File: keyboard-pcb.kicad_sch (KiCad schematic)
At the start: 3 parts, among them P1 USB_C_Plug_USB2.0, U1 RP2040, U2 XC6206PxxxMR

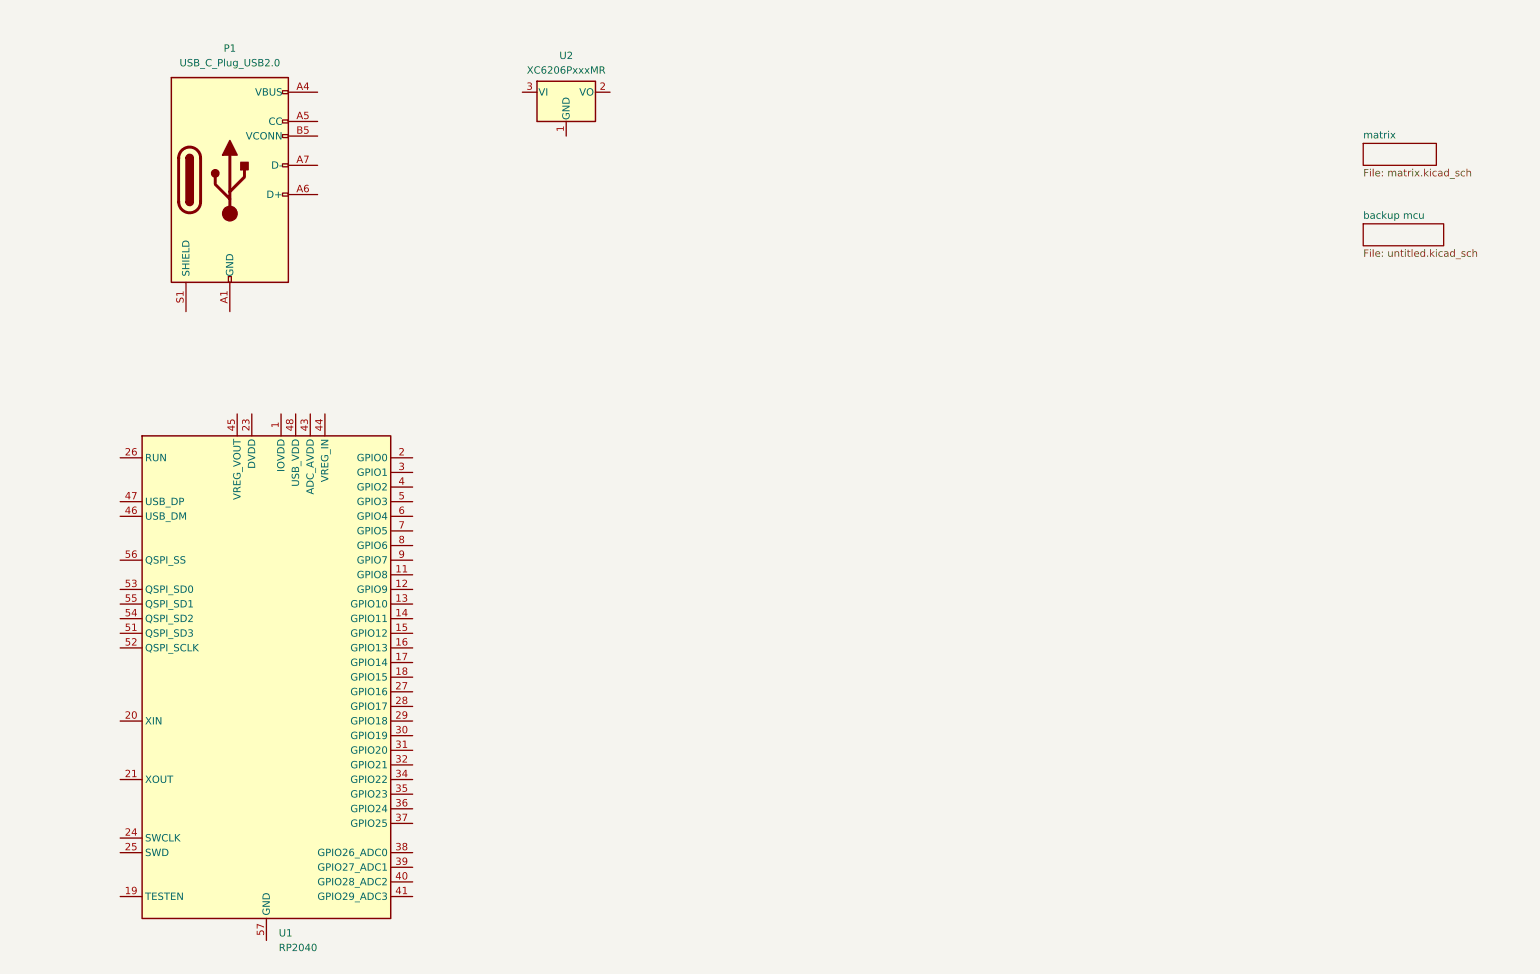
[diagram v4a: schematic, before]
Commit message: Assigned footprints to components
Also edited layout slightly (7u spacebar and removal of PrtSc, ScLk, Pause)
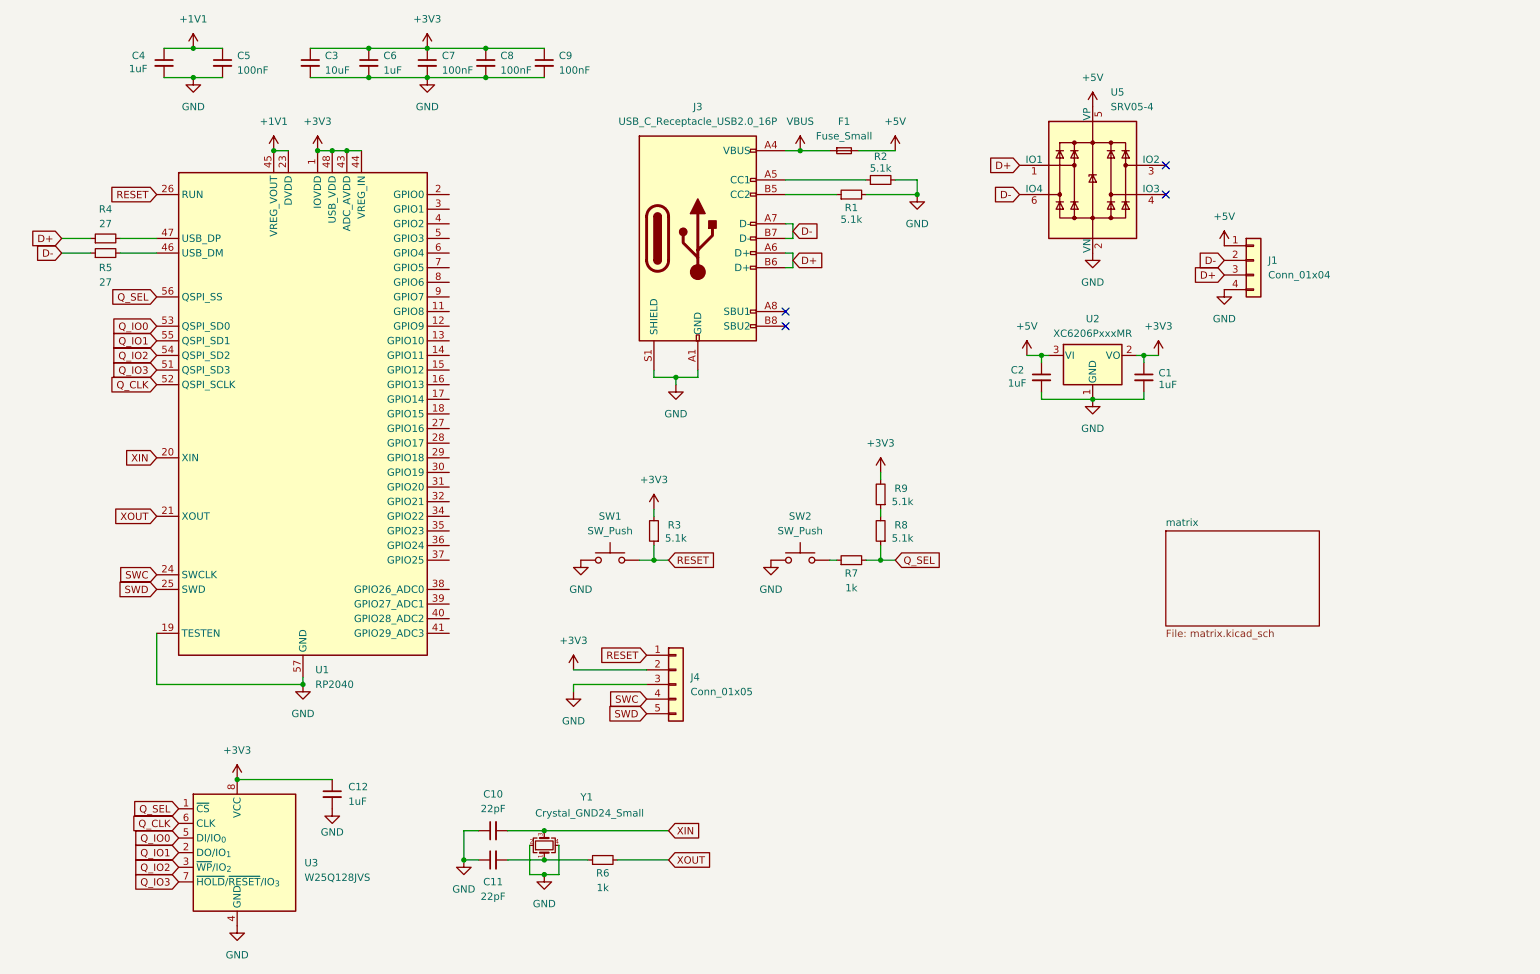
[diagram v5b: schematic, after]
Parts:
- removed P1: USB_C_Plug_USB2.0, symbol Connector:USB_C_Plug_USB2.0
- added C1, C12, C2, C4, C6: 1uF, Capacitor_SMD:C_0805_2012Metric, symbol Device:C_Small
- added C10, C11: 22pF, Capacitor_SMD:C_0805_2012Metric, symbol Device:C_Small
- added C3: 10uF, Capacitor_SMD:C_0805_2012Metric, symbol Device:C_Small
- added C5, C7, C8, C9: 100nF, Capacitor_SMD:C_0805_2012Metric, symbol Device:C_Small
- added F1: Fuse_Small, Fuse:Fuse_1206_3216Metric, symbol Device:Fuse_Small
- added J1: Conn_01x04, Connector_JST:JST_SH_SM04B-SRSS-TB_1x04-1MP_P1.00mm_Horizontal, symbol Connector_Generic:Conn_01x04
- added J3: USB_C_Receptacle_USB2.0_16P, Connector_USB:USB_C_Receptacle_HRO_TYPE-C-31-M-12, symbol Connector:USB_C_Receptacle_USB2.0_16P
- added J4: Conn_01x05, Connector_PinHeader_2.54mm:PinHeader_1x05_P2.54mm_Vertical, symbol Connector_Generic:Conn_01x05
- added R1, R2, R3, R8, R9: 5.1k, Resistor_SMD:R_0805_2012Metric, symbol Device:R_Small
- added R4, R5: 27, Resistor_SMD:R_0805_2012Metric, symbol Device:R_Small
- added R6, R7: 1k, Resistor_SMD:R_0805_2012Metric, symbol Device:R_Small
- added SW1, SW2: SW_Push, Button_Switch_SMD:SW_SPST_TL3342, symbol Switch:SW_Push
- added U3: W25Q128JVS, Package_SO:SOIC-8_5.3x5.3mm_P1.27mm, symbol Memory_Flash:W25Q128JVS
- added U5: SRV05-4, PCM_marbastlib-various:SOT-23-6-routable, symbol PCM_marbastlib-various:SRV05-4
- added Y1: Crystal_GND24_Small, Crystal:Crystal_SMD_3225-4Pin_3.2x2.5mm, symbol Device:Crystal_GND24_Small
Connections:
- net +3V3: now reaches U1.1 (IOVDD), U1.10 (IOVDD), U1.22 (IOVDD), U1.33 (IOVDD), U1.42 (IOVDD), U1.49 (IOVDD)
- net +3V3: now also U1.43 (ADC_AVDD), U1.44 (VREG_IN), U1.48 (USB_VDD), U2.2 (VO), C1.1, C12.1, C3.1, C6.1, C7.1, C8.1, C9.1, J4.2 (Pin_2), R3.2, R9.2, U3.8 (VCC)
- net GND: now reaches U1.19 (TESTEN)
- net GND: now also U1.57 (GND), U2.1 (GND), C1.2, C10.1, C11.1, C12.2, C2.2, C3.2, C4.2, C5.2, C6.2, C7.2, C8.2, C9.2, J1.4 (Pin_4), J3.A1 (GND), J3.A12 (GND), J3.B1 (GND), J3.B12 (GND), J3.S1 (SHIELD), J4.3 (Pin_3), R1.2, R2.2, SW1.1, SW2.1, U3.4 (GND), U5.2 (VN), Y1.2, Y1.4
- net XIN: now reaches U1.20 (XIN)
- net XIN: now also C10.2, Y1.3
- net XOUT: now reaches U1.21 (XOUT)
- net XOUT: now also R6.2
- net +1V1: now reaches U1.23 (DVDD), U1.50 (DVDD)
- net +1V1: now also U1.45 (VREG_VOUT), C4.1, C5.1
- net SWC: now reaches U1.24 (SWCLK)
- net SWC: now also J4.4 (Pin_4)
- net SWD: now reaches U1.25 (SWD)
- net SWD: now also J4.5 (Pin_5)
- net RESET: now reaches U1.26 (RUN)
- net RESET: now also J4.1 (Pin_1), R3.1, SW1.2
- net at U1.46 (USB_DM): now also R5.2
- net at U1.47 (USB_DP): now also R4.2
- net Q_IO3: now reaches U1.51 (QSPI_SD3)
- net Q_IO3: now also U3.7 (~{HOLD}/~{RESET}/IO_{3})
- net Q_CLK: now reaches U1.52 (QSPI_SCLK)
- net Q_CLK: now also U3.6 (CLK)
- net Q_IO0: now reaches U1.53 (QSPI_SD0)
- net Q_IO0: now also U3.5 (DI/IO_{0})
- net Q_IO2: now reaches U1.54 (QSPI_SD2)
- net Q_IO2: now also U3.3 (~{WP}/IO_{2})
- net Q_IO1: now reaches U1.55 (QSPI_SD1)
- net Q_IO1: now also U3.2 (DO/IO_{1})
- net Q_SEL: now reaches U1.56 (QSPI_SS)
- net Q_SEL: now also R7.2, R8.1, U3.1 (~{CS})
- net +5V: now reaches U2.3 (VI)
- net +5V: now also C2.1, F1.2, J1.1 (Pin_1), U5.5 (VP)
- new net: R7.1, SW2.2
- new net: J3.B5 (CC2), R1.1
- new net: J3.A5 (CC1), R2.1
- new net: R8.2, R9.1
- new net: C11.2, R6.1, Y1.1
- new net D+: J1.3 (Pin_3), J3.A6 (D+), J3.B6 (D+), R4.1, U5.1 (IO1)
- new net D-: J1.2 (Pin_2), J3.A7 (D-), J3.B7 (D-), R5.1, U5.6 (IO4)
- new net VBUS: F1.1, J3.A4 (VBUS), J3.A9 (VBUS), J3.B4 (VBUS), J3.B9 (VBUS)
- no-connect marks 0 -> 4
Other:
- removed sheet backup mcu
- title: (none) -> TKL Keyboard PCB
- moved on the sheet: U1, U2
